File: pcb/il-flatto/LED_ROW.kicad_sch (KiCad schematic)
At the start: 9 parts

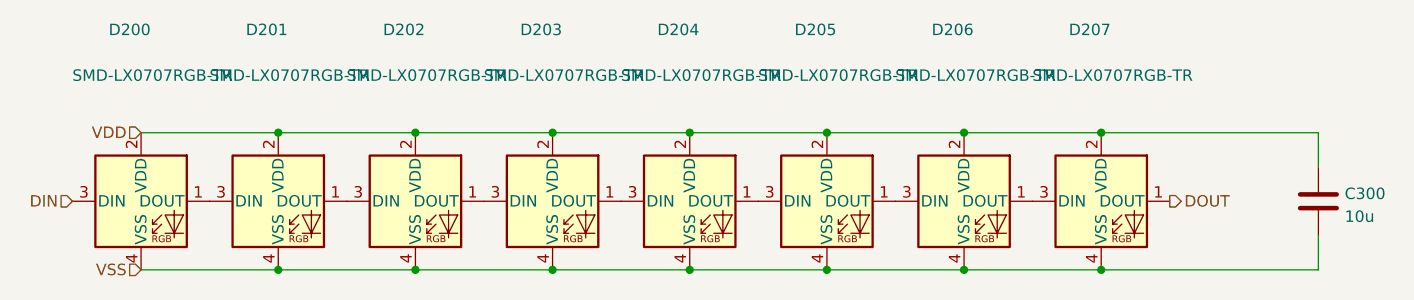
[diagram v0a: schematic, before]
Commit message: changed to 1.5mm RGBLEDs because cheaper
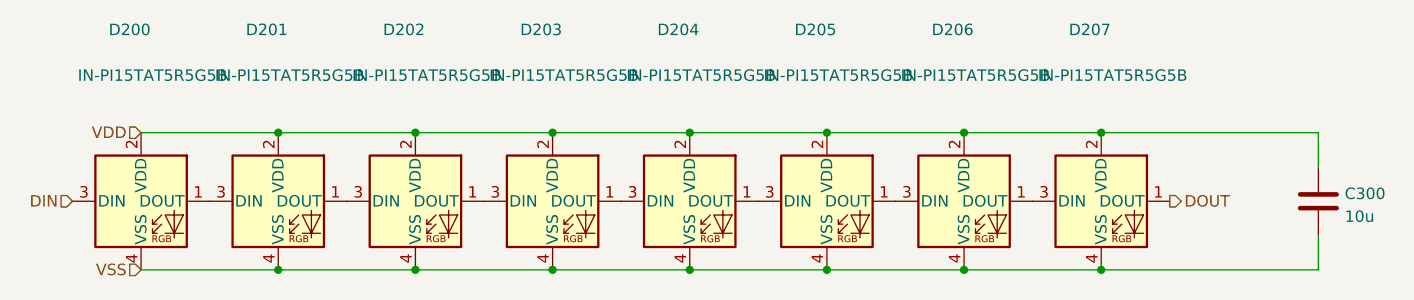
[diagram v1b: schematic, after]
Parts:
- D200, D201, D202, D203, D204, D205, D206, D207: value SMD-LX0707RGB-TR -> IN-PI15TAT5R5G5B; footprint footprints:SMD-LX0707RGB-TR -> footprints:INPI15TAT5R5G5B
